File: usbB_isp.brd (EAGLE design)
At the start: 100 x 80 mm, 12 parts, among them IC1 788TV, IC2 TINY13-20PU, X1 PN61729-S

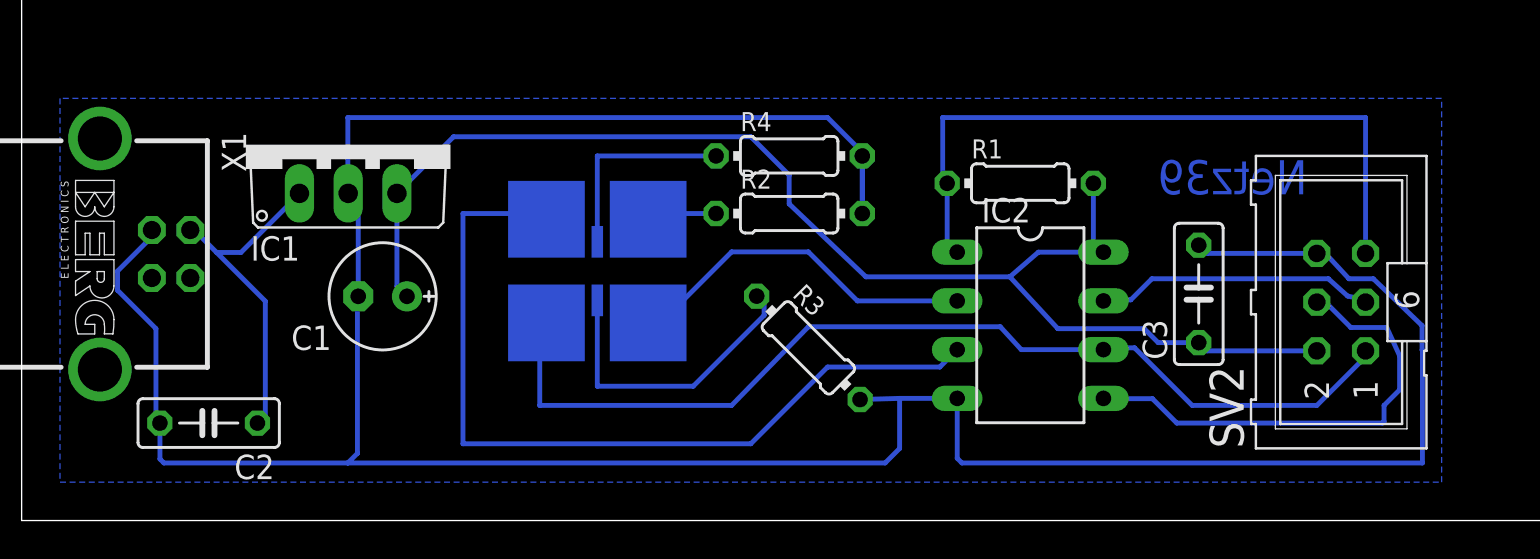
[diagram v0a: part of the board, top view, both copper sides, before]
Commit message: reroute, using 16 mil wires
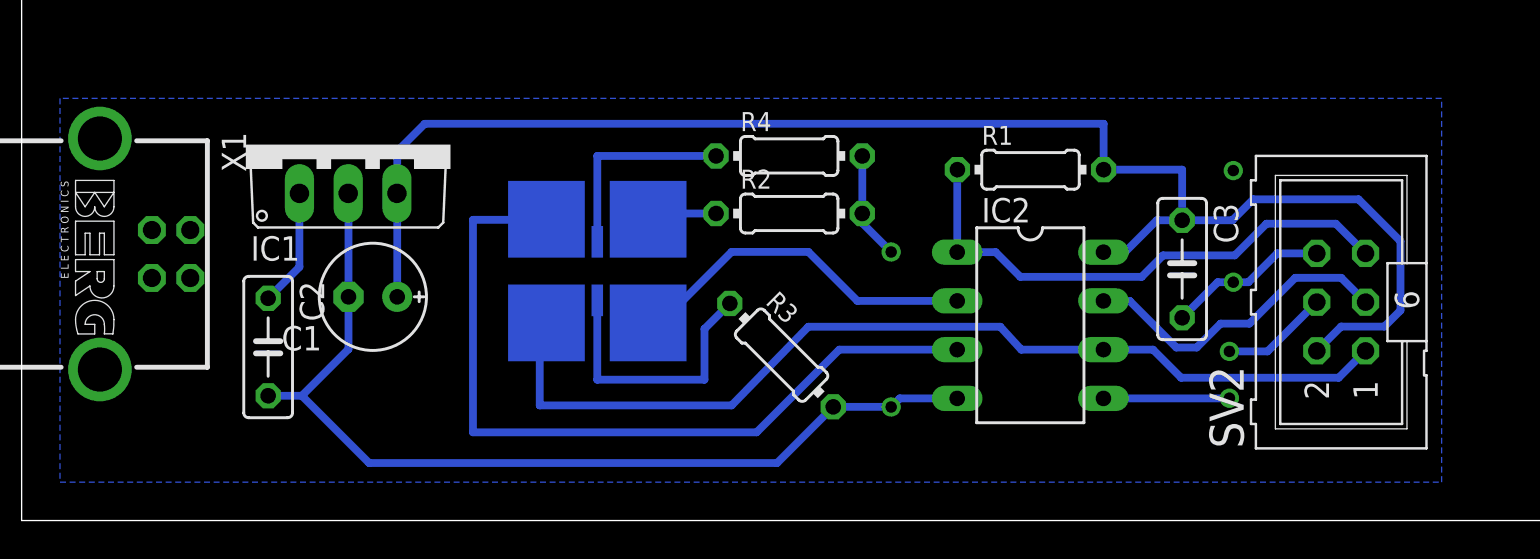
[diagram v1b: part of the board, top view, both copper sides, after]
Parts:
- moved C2 5.03 mm to (12.8, 9.04), turned to 270 degrees
- moved C3 1.56 mm to (60.5, 13.1), turned to 270 degrees
- moved R3 1.45 mm to (39.6, 8.62)
- moved R1 0.89 mm to (52.6, 18.3)
- moved C1 0.51 mm to (18.3, 11.7)
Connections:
- net N$10 renamed MOSI
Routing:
- net GND: track 160.4 -> 64.4 mm, vias 0 -> 4
- net MOSI: track 24.8 -> 12.2 mm, vias 0 -> 2
- net N$1: track 17.9 -> 6.14 mm
- net VCC: track 69.4 -> 80.5 mm
- net _RESET: track 36.6 -> 27.9 mm
- net N$9: track 46.3 -> 42.0 mm
- net SCK: track 14.6 -> 16.7 mm
- net N$7: track 16.1 -> 14.2 mm
- net MISO: track 52.4 -> 50.9 mm
- added copper zone on layer 16, net GND
- removed copper zone on layer 16, net N$2
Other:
- board text removed: "Netz39"

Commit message: adapted design rules and fixed some design rule check issues
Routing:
- net GND: track 64.4 -> 78.3 mm
- net MOSI: track 12.2 -> 14.7 mm
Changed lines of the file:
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@@
 </class>
 </classes>
-<designrules name="default">
+<designrules name="default *">
 <description language="de">&lt;b&gt;EAGLE Design Rules&lt;/b&gt;
 &lt;p&gt;
@@
 <param name="mtCopper" value="0.035mm 0.035mm 0.035mm 0.035mm 0.035mm 0.035mm 0.035mm 0.035mm 0.035mm 0.035mm 0.035mm 0.035mm 0.035mm 0.035mm 0.035mm 0.035mm"/>
 <param name="mtIsolate" value="1.5mm 0.15mm 0.2mm 0.15mm 0.2mm 0.15mm 0.2mm 0.15mm 0.2mm 0.15mm 0.2mm 0.15mm 0.2mm 0.15mm 0.2mm"/>
-<param name="mdWireWire" value="8mil"/>
-<param name="mdWirePad" value="8mil"/>
-<param name="mdWireVia" value="8mil"/>
-<param name="mdPadPad" value="8mil"/>
-<param name="mdPadVia" value="8mil"/>
-<param name="mdViaVia" value="8mil"/>
-<param name="mdSmdPad" value="8mil"/>
-<param name="mdSmdVia" value="8mil"/>
-<param name="mdSmdSmd" value="8mil"/>
+<param name="mdWireWire" value="12mil"/>
+<param name="mdWirePad" value="12mil"/>
+<param name="mdWireVia" value="12mil"/>
+<param name="mdPadPad" value="12mil"/>
+<param name="mdPadVia" value="12mil"/>
+<param name="mdViaVia" value="12mil"/>
+<param name="mdSmdPad" value="12mil"/>
+<param name="mdSmdVia" value="12mil"/>
+<param name="mdSmdSmd" value="12mil"/>
 <param name="mdViaViaSameLayer" value="8mil"/>
 <param name="mnLayersViaInSmd" value="2"/>
 <param name="mdCopperDimension" value="40mil"/>
-<param name="mdDrill" value="8mil"/>
+<param name="mdDrill" value="12mil"/>
 <param name="mdSmdStop" value="0mil"/>
-<param name="msWidth" value="10mil"/>
+<param name="msWidth" value="12mil"/>
 <param name="msDrill" value="24mil"/>
 <param name="msMicroVia" value="9.99mm"/>
@@
 <param name="rvMicroViaOuter" value="0.25"/>
 <param name="rvMicroViaInner" value="0.25"/>
-<param name="rlMinPadTop" value="10mil"/>
+<param name="rlMinPadTop" value="12mil"/>
 <param name="rlMaxPadTop" value="20mil"/>
 <param name="rlMinPadInner" value="10mil"/>
 <param name="rlMaxPadInner" value="20mil"/>
-<param name="rlMinPadBottom" value="10mil"/>
+<param name="rlMinPadBottom" value="12mil"/>
 <param name="rlMaxPadBottom" value="20mil"/>
-<param name="rlMinViaOuter" value="8mil"/>
+<param name="rlMinViaOuter" value="12mil"/>
 <param name="rlMaxViaOuter" value="20mil"/>
 <param name="rlMinViaInner" value="8mil"/>
@@
 <wire x1="42.297075" y1="5.924921875" x2="39.369353125" y2="2.9972" width="0.4064" layer="16"/>
 <wire x1="39.369353125" y1="2.9972" x2="18.1102" y2="2.9972" width="0.4064" layer="16"/>
-<polygon width="0.254" layer="16" isolate="0.254">
+<polygon width="0.4064" layer="16" isolate="0.4064" thermals="no">
 <vertex x="2" y="22"/>
 <vertex x="2" y="2"/>
@@
 <vertex x="74" y="22"/>
 </polygon>
-<wire x1="65.4332" y1="13.922" x2="63.1444" y2="18.2372" width="0" layer="19" extent="16-16"/>
+<wire x1="63.1444" y1="18.2372" x2="63.1444" y2="12.4206" width="0.4064" layer="1"/>
+<wire x1="45.3136" y1="13.9954" x2="45.3136" y2="5.9182" width="0.4064" layer="1"/>
 </signal>
 <signal name="VCC">
@@
 <contactref element="SV2" pad="1"/>
 <wire x1="56.376" y1="8.906" x2="52.094" y2="8.906" width="0.4064" layer="16"/>
-<wire x1="52.094" y1="8.906" x2="51" y2="10.1" width="0.4064" layer="16"/>
-<wire x1="51" y1="10.1" x2="41" y2="10.1" width="0.4064" layer="16"/>
-<wire x1="41" y1="10.1" x2="37" y2="6" width="0.4064" layer="16"/>
+<wire x1="52.094" y1="8.906" x2="51" y2="10.1508" width="0.4064" layer="16"/>
+<wire x1="51" y1="10.1508" x2="41" y2="10.1508" width="0.4064" layer="16"/>
+<wire x1="41" y1="10.1508" x2="37" y2="6" width="0.4064" layer="16"/>
 <wire x1="37" y1="6" x2="27" y2="6" width="0.4064" layer="16"/>
 <wire x1="27" y1="6" x2="27" y2="10" width="0.4064" layer="16"/>
 <wire x1="27" y1="10" x2="27.05" y2="10" width="0.254" layer="16"/>
 <wire x1="27.05" y1="10" x2="27.35" y2="10.3" width="0.254" layer="16"/>
-<wire x1="70.036" y1="8.842" x2="68.6362" y2="7.4422" width="0.4064" layer="16"/>
-<wire x1="68.6362" y1="7.4422" x2="60.4266" y2="7.4422" width="0.4064" layer="16"/>
-<wire x1="60.4266" y1="7.4422" x2="58.9628" y2="8.906" width="0.4064" layer="16"/>
+<wire x1="70.036" y1="8.842" x2="68.6362" y2="7.5184" width="0.4064" layer="16"/>
+<wire x1="68.6362" y1="7.5184" x2="60.4266" y2="7.5184" width="0.4064" layer="16"/>
+<wire x1="60.4266" y1="7.5184" x2="58.9628" y2="8.906" width="0.4064" layer="16"/>
 <wire x1="58.9628" y1="8.906" x2="56.376" y2="8.906" width="0.4064" layer="16"/>
 </signal>
@@
 <contactref element="SV2" pad="4"/>
 <wire x1="67.496" y1="11.382" x2="64.9278" y2="8.8138" width="0.4064" layer="16"/>
-<via x="62.9412" y="8.8138" extent="1-16" drill="0.6" shape="square"/>
-<via x="62.9412" y="6.3754" extent="1-16" drill="0.6" shape="square"/>
-<wire x1="62.9412" y1="8.8138" x2="64.9278" y2="8.8138" width="0.4064" layer="16"/>
+<via x="62.9666" y="8.8138" extent="1-16" drill="0.6" shape="square"/>
+<via x="62.992" y="6.3754" extent="1-16" drill="0.6" shape="square"/>
+<wire x1="62.9666" y1="8.8138" x2="64.9278" y2="8.8138" width="0.4064" layer="16"/>
 <wire x1="56.376" y1="6.366" x2="62.9412" y2="6.366" width="0.4064" layer="16"/>
-<wire x1="62.9412" y1="6.366" x2="62.9412" y2="6.3754" width="0.4064" layer="16"/>
-<wire x1="62.9412" y1="6.3754" x2="62.9412" y2="8.8138" width="0" layer="19" extent="1-1"/>
+<wire x1="62.9412" y1="6.366" x2="62.992" y2="6.3754" width="0.4064" layer="16"/>
+<wire x1="62.992" y1="6.3754" x2="62.9666" y2="6.3754" width="0.4064" layer="1"/>
+<wire x1="62.9666" y1="6.3754" x2="62.9666" y2="8.8138" width="0.4064" layer="1"/>
 </signal>
 <signal name="SCK">
@@
 </signal>
 </signals>
+<errors>
+</errors>
 </board>
 </drawing>
